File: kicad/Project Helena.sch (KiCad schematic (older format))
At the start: 63 parts, among them J1 Conn_01x24, SW1 SW_SPST, SW10 H, SW11 SPACE, SW12 HELP, SW13 8, SW14 5, SW15 I, SW16 T, SW17 K, SW18 G, SW19 M, SW2 SW_SPST, SW20 B, SW21 SW_SPST, SW22 9, SW23 4, SW24 O, SW25 R, SW26 L, SW27 F, SW28 COMMA, SW29 V, SW3 SW_SPST, SW30 SW_SPST, SW31 0, SW32 3, SW33 P, SW34 E, SW35 SEMICOLON, SW36 D, SW37 PERIOD, SW38 C, SW39 SW_SPST, SW4 7, SW40 <, SW41 2, SW42 MINUS, SW43 W, SW44 PLUS, SW45 S, SW46 SLASH, SW47 X, SW48 SW_SPST, SW49 >, SW5 6, SW50 1, SW51 EQUAL, SW52 Q, SW53 ASTERISK, SW54 A, SW55 INV, SW56 Z, SW57 DEL, SW58 ESC, SW59 RETURN, SW6 U, SW60 TAB, SW61 CAPS, SW7 Y, SW8 N, SW9 J

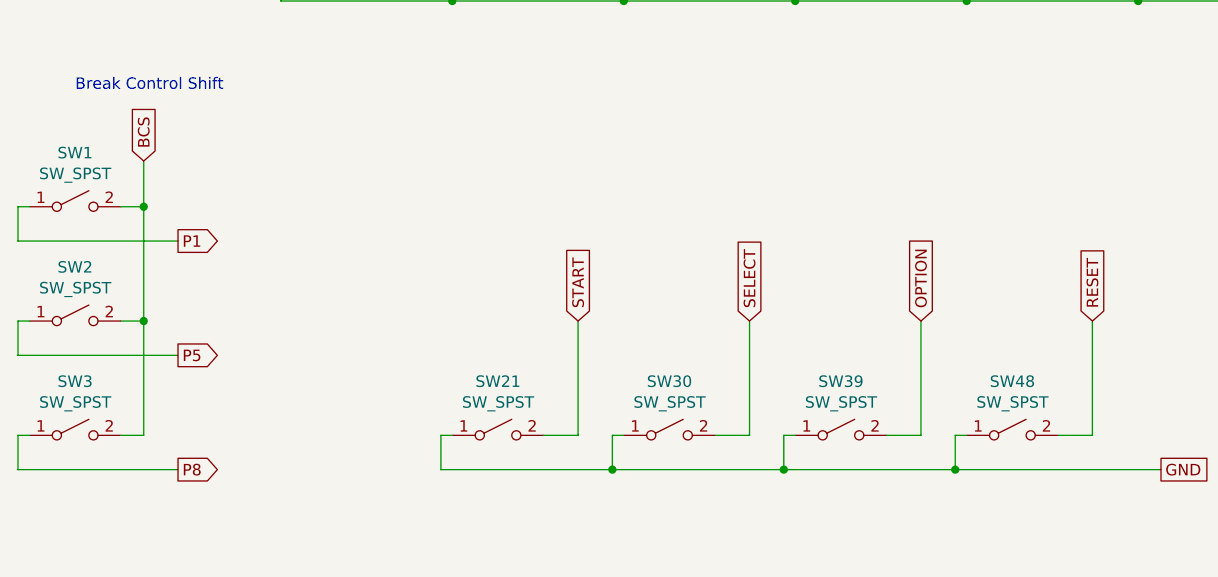
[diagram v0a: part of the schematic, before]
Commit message: add labels for BCS and SSOR.
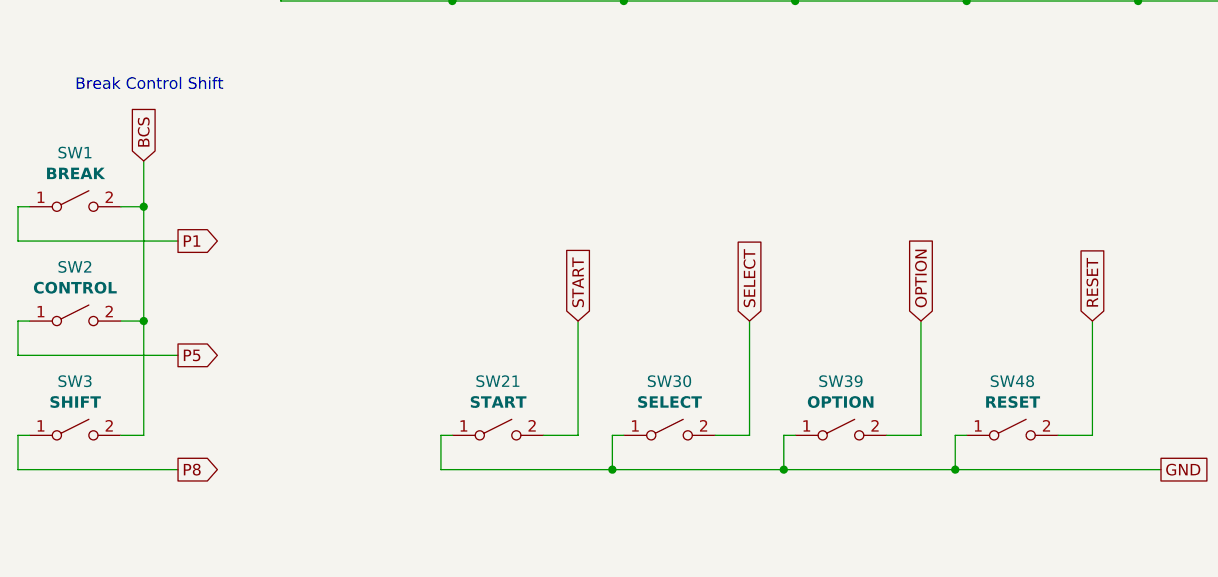
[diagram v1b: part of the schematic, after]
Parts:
- SW1: value SW_SPST -> BREAK
- SW2: value SW_SPST -> CONTROL
- SW21: value SW_SPST -> START
- SW3: value SW_SPST -> SHIFT
- SW30: value SW_SPST -> SELECT
- SW39: value SW_SPST -> OPTION
- SW48: value SW_SPST -> RESET
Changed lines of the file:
@@
 EESchema Schematic File Version 4
+LIBS:Project Helena-cache
 EELAYER 26 0
 EELAYER END
@@
 P 1300 6050
 F 0 "SW1" H 1300 6285 50  0000 C CNN
-F 1 "SW_SPST" H 1300 6194 50  0000 C CNN
+F 1 "BREAK" H 1300 6194 50  0000 C CNB
 F 2 "" H 1300 6050 50  0001 C CNN
 F 3 "" H 1300 6050 50  0001 C CNN
@@
 P 1300 6550
 F 0 "SW2" H 1300 6785 50  0000 C CNN
-F 1 "SW_SPST" H 1300 6694 50  0000 C CNN
+F 1 "CONTROL" H 1300 6694 50  0000 C CNB
 F 2 "" H 1300 6550 50  0001 C CNN
 F 3 "" H 1300 6550 50  0001 C CNN
@@
 P 1300 7050
 F 0 "SW3" H 1300 7285 50  0000 C CNN
-F 1 "SW_SPST" H 1300 7194 50  0000 C CNN
+F 1 "SHIFT" H 1300 7194 50  0000 C CNB
 F 2 "" H 1300 7050 50  0001 C CNN
 F 3 "" H 1300 7050 50  0001 C CNN
@@
 P 3150 7050
 F 0 "SW21" H 3150 7285 50  0000 C CNN
-F 1 "SW_SPST" H 3150 7194 50  0000 C CNN
+F 1 "START" H 3150 7194 50  0000 C CNB
 F 2 "" H 3150 7050 50  0001 C CNN
 F 3 "" H 3150 7050 50  0001 C CNN
@@
 P 3900 7050
 F 0 "SW30" H 3900 7285 50  0000 C CNN
-F 1 "SW_SPST" H 3900 7194 50  0000 C CNN
+F 1 "SELECT" H 3900 7194 50  0000 C CNB
 F 2 "" H 3900 7050 50  0001 C CNN
 F 3 "" H 3900 7050 50  0001 C CNN
@@
 P 4650 7050
 F 0 "SW39" H 4650 7285 50  0000 C CNN
-F 1 "SW_SPST" H 4650 7194 50  0000 C CNN
+F 1 "OPTION" H 4650 7194 50  0000 C CNB
 F 2 "" H 4650 7050 50  0001 C CNN
 F 3 "" H 4650 7050 50  0001 C CNN
@@
 P 5400 7050
 F 0 "SW48" H 5400 7285 50  0000 C CNN
-F 1 "SW_SPST" H 5400 7194 50  0000 C CNN
+F 1 "RESET" H 5400 7194 50  0000 C CNB
 F 2 "" H 5400 7050 50  0001 C CNN
 F 3 "" H 5400 7050 50  0001 C CNN

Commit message: first revision of PCB
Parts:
- added J2, J3: Conn_01x08, Connector_PinHeader_2.54mm:PinHeader_1x08_P2.54mm_Vertical, symbol Connector_Generic:Conn_01x08
- added SW62, SW63: SPACE, Button_Switch_Keyboard:SW_Cherry_MX1A_1.00u_Plate, symbol Switch:SW_SPST
- added SW64: SHIFT_R, Button_Switch_Keyboard:SW_Cherry_MX1A_1.75u_Plate, symbol Switch:SW_SPST
- D1: footprint (none) -> LED_THT:LED_D5.0mm
- J1: footprint (none) -> Connector_PinSocket_2.54mm:PinSocket_1x24_P2.54mm_Vertical
- SW1, SW10, SW11, SW12, SW13, SW14, SW15, SW16, SW17, SW18, SW19, SW20, SW21, SW22, SW23, SW24, SW25, SW26, SW27, SW28, SW29, SW30, SW31, SW32, SW33, SW34, SW35, SW36, SW37, SW38, SW39, SW4, SW40, SW41, SW42, SW43, SW44, SW45, SW46, SW47, SW48, SW49, SW5, SW50, SW51, SW52, SW53, SW54, SW55, SW56, SW57, SW6, SW7, SW8, SW9: footprint (none) -> Button_Switch_Keyboard:SW_Cherry_MX1A_1.00u_Plate
- SW2: footprint (none) -> Button_Switch_Keyboard:SW_Cherry_MX1A_2.00u_Plate
- SW3: value SHIFT -> SHIFT_L; footprint (none) -> Button_Switch_Keyboard:SW_Cherry_MX1A_1.50u_Plate
- SW58, SW61: footprint (none) -> Button_Switch_Keyboard:SW_Cherry_MX1A_1.25u_Plate
- SW59: footprint (none) -> Button_Switch_Keyboard:SW_Cherry_MX1A_1.50u_Plate
- SW60: footprint (none) -> Button_Switch_Keyboard:SW_Cherry_MX1A_1.75u_Plate
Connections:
- net BCS: now also SW64.2 (B)
- net GND: now also J2.1 (Pin_1); no longer D1.1 (K), SW21.1 (A), SW30.1 (A), SW39.1 (A), SW48.1 (A)
- net LED: now also J2.8 (Pin_8); no longer D1.2 (A)
- net OPTION: now also J2.4 (Pin_4); no longer SW39.2 (B)
- net P11: now also J2.6 (Pin_6), SW62.2 (B), SW63.2 (B); no longer SW12.2 (B)
- net P7: now also SW62.1 (A), SW63.1 (A)
- net P8: now also J2.7 (Pin_7), SW64.1 (A); no longer SW12.1 (A)
- net RESET: now also J2.5 (Pin_5); no longer SW48.2 (B)
- net SELECT: now also J2.3 (Pin_3); no longer SW30.2 (B)
- net START: now also J2.2 (Pin_2); no longer SW21.2 (B)
- new net WIRE_GND: D1.1 (K), J3.1 (Pin_1), SW21.1 (A), SW30.1 (A), SW39.1 (A), SW48.1 (A)
- new net WIRE_LED: D1.2 (A), J3.8 (Pin_8)
- new net WIRE_OPTION: J3.4 (Pin_4), SW39.2 (B)
- new net WIRE_P11: J3.6 (Pin_6), SW12.2 (B)
- new net WIRE_P8: J3.7 (Pin_7), SW12.1 (A)
- new net WIRE_RESET: J3.5 (Pin_5), SW48.2 (B)
- new net WIRE_SELECT: J3.3 (Pin_3), SW30.2 (B)
- new net WIRE_START: J3.2 (Pin_2), SW21.2 (B)
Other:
- moved on the sheet: D1

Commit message: update silkscreen!
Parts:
- J1: footprint Connector_PinSocket_2.54mm:PinSocket_1x24_P2.54mm_Vertical -> Connector_PinHeader_2.54mm:PinHeader_1x24_P2.54mm_Vertical
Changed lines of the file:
@@
 F 0 "J1" H 10280 1992 50  0000 L CNN
 F 1 "Conn_01x24" H 10280 1901 50  0000 L CNN
-F 2 "Connector_PinSocket_2.54mm:PinSocket_1x24_P2.54mm_Vertical" H 10200 2000 50  0001 C CNN
+F 2 "Connector_PinHeader_2.54mm:PinHeader_1x24_P2.54mm_Vertical" H 10200 2000 50  0001 C CNN
 F 3 "~" H 10200 2000 50  0001 C CNN
 	1    10200 2000
